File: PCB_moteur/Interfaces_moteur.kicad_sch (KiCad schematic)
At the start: 3 parts, among them Q1 BSS138, U3 LSF0102DCUR

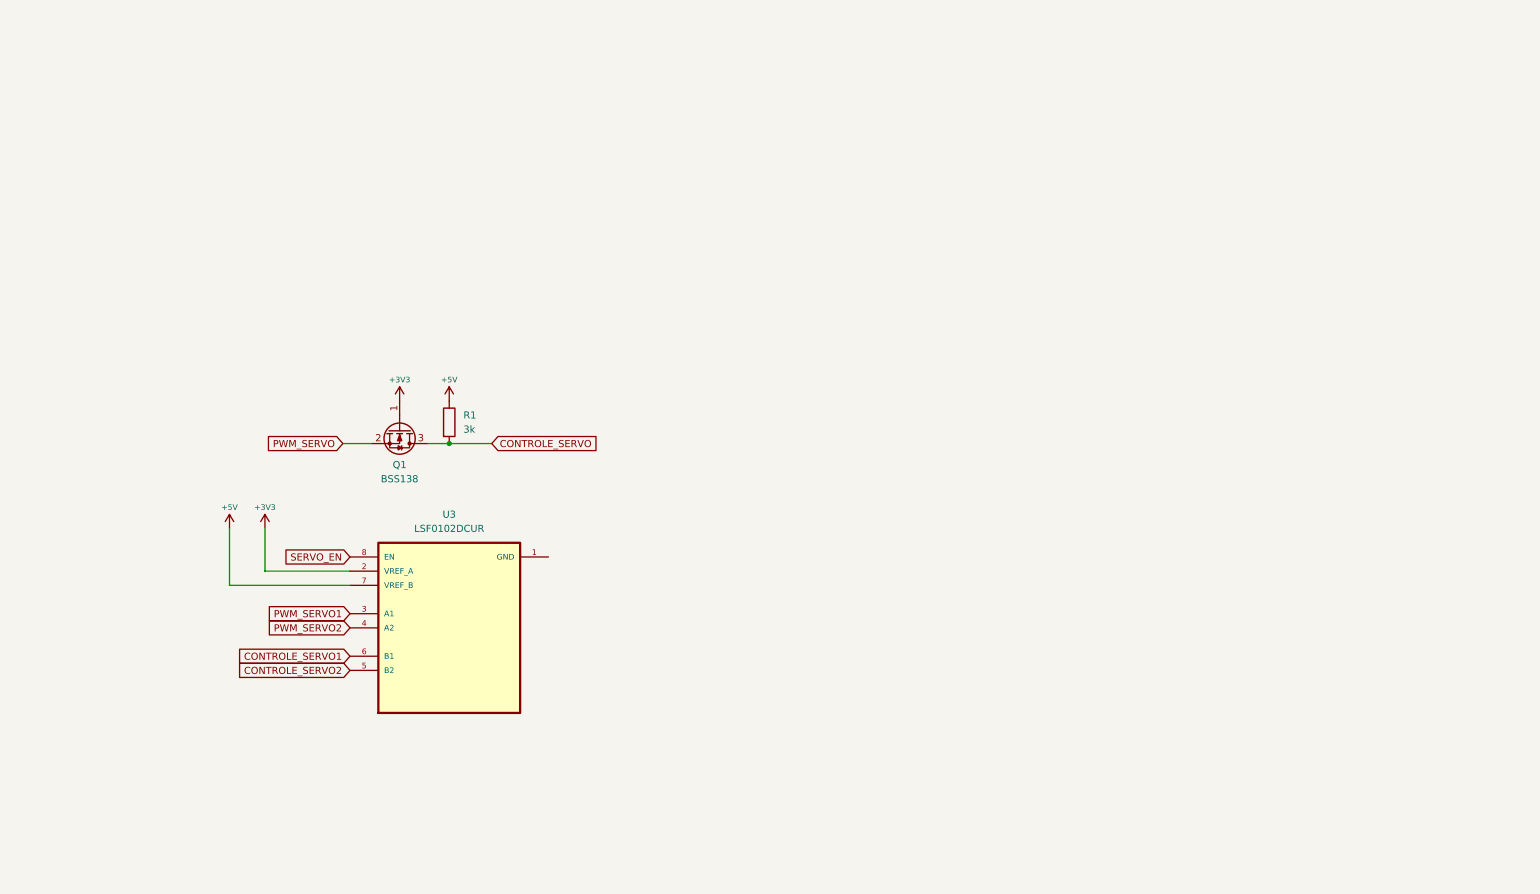
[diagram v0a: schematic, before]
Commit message: Manque supply, pyro et finition (découplage etc)
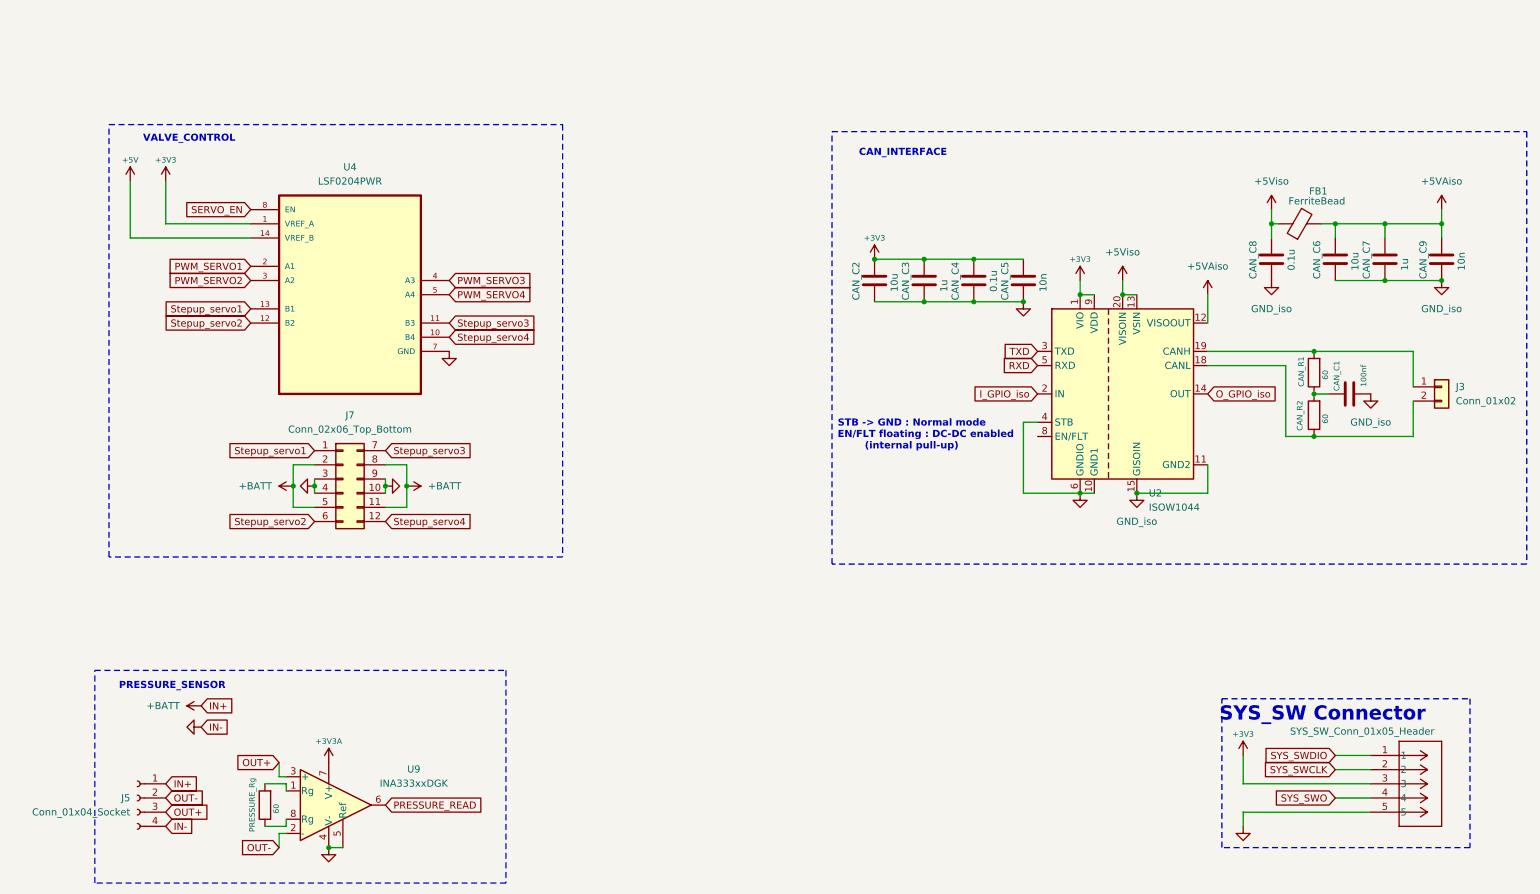
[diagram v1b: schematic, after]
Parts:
- removed Q1: BSS138, Package_TO_SOT_SMD:SOT-23, symbol Transistor_FET:BSS138
- removed R1: 3k, symbol Device:R
- removed U3: LSF0102DCUR, LSF0102DCUR:SOP50P310X90-8N, symbol LSF0102DCUR:LSF0102DCUR
- added CAN_C1: 100nf, Capacitor_SMD:C_0805_2012Metric, symbol Device:C
- added CAN_C2, CAN_C6: 10u, symbol Device:C
- added CAN_C3, CAN_C7: 1u, symbol Device:C
- added CAN_C4, CAN_C8: 0.1u, symbol Device:C
- added CAN_C5, CAN_C9: 10n, symbol Device:C
- added CAN_R1, CAN_R2, PRESSURE_Rg: 60, Resistor_SMD:R_0805_2012Metric, symbol Device:R
- added FB1: FerriteBead, symbol Device:FerriteBead
- added J3: Conn_01x02, symbol Connector_Generic:Conn_01x02
- added J4: SYS_SW_Conn_01x05_Header, Connector_PinHeader_2.54mm:PinHeader_1x05_P2.54mm_Vertical, symbol ODB2:705430004
- added J5: Conn_01x04_Socket, symbol Connector:Conn_01x04_Socket
- added J7: Conn_02x06_Top_Bottom, symbol Connector_Generic:Conn_02x06_Top_Bottom
- added U2: ISOW1044, Package_SO:SOIC-20W_7.5x12.8mm_P1.27mm, symbol Interface_CAN_LIN:ISOW1044
- added U4: LSF0204PWR, LSF0204PWR:SOP65P640X120-14N, symbol LSF0204PWR:LSF0204PWR
- added U9: INA333xxDGK, Package_SO:VSSOP-8_3x3mm_P0.65mm, symbol Amplifier_Instrumentation:INA333xxDGK
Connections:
- net +3V3: now also CAN_C2.1, CAN_C3.1, CAN_C4.1, CAN_C5.1, J4.3, U2.1 (VIO), U2.9 (VDD), U4.1 (VREF_A)
- net +5V: now also U4.14 (VREF_B)
- net PWM_SERVO1: now also U4.2 (A1)
- net PWM_SERVO2: now also U4.3 (A2)
- net SERVO_EN: now also U4.8 (EN)
- new net: PRESSURE_Rg.2, U9.1 (Rg)
- new net: PRESSURE_Rg.1, U9.8 (Rg)
- new net: CAN_R2.1, J3.2 (Pin_2), U2.18 (CANL)
- new net: CAN_C1.1, CAN_R1.1, CAN_R2.2
- new net: CAN_R1.2, J3.1 (Pin_1), U2.19 (CANH)
- new net +3V3A: U9.7 (V+)
- new net +5VAiso: CAN_C6.1, CAN_C7.1, CAN_C9.1, FB1.2, U2.12 (VISOOUT)
- new net +5Viso: CAN_C8.1, FB1.1, U2.13 (VSIN), U2.20 (VISOIN)
- new net +BATT: J5.1 (Pin_1), J7.11 (Pin_11), J7.2 (Pin_2), J7.5 (Pin_5), J7.8 (Pin_8)
- new net GND: CAN_C2.2, CAN_C3.2, CAN_C4.2, CAN_C5.2, J4.5, J5.4 (Pin_4), J7.10 (Pin_10), J7.3 (Pin_3), J7.4 (Pin_4), J7.9 (Pin_9), U2.10 (GND1), U2.4 (STB), U2.6 (GNDIO), U4.7 (GND), U9.4 (V-), U9.5 (Ref)
- new net GND_iso: CAN_C1.2, CAN_C6.2, CAN_C7.2, CAN_C8.2, CAN_C9.2, U2.11 (GND2), U2.15 (GISOIN), U2.16 (GISOIN), U2.17 (GISOIN)
- new net I_GPIO_iso: U2.2 (IN)
- new net OUT+: J5.3 (Pin_3), U9.3 (+)
- new net OUT-: J5.2 (Pin_2), U9.2 (-)
- new net O_GPIO_iso: U2.14 (OUT)
- new net PRESSURE_READ: U9.6
- new net PWM_SERVO3: U4.4 (A3)
- new net PWM_SERVO4: U4.5 (A4)
- new net RXD: U2.5 (RXD)
- new net SYS_SWCLK: J4.2
- new net SYS_SWDIO: J4.1
- new net SYS_SWO: J4.4
- new net Stepup_servo1: J7.1 (Pin_1), U4.13 (B1)
- new net Stepup_servo2: J7.6 (Pin_6), U4.12 (B2)
- new net Stepup_servo3: J7.7 (Pin_7), U4.11 (B3)
- new net Stepup_servo4: J7.12 (Pin_12), U4.10 (B4)
- new net TXD: U2.3 (TXD)
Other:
- note added: "CAN_INTERFACE"
- note added: "PRESSURE_SENSOR"
- note added: "STB -> GND : Normal mode EN/FLT floating : DC-DC enabled (internal pull-up)"
- note added: "SYS_SW Connector"
- note added: "VALVE_CONTROL"

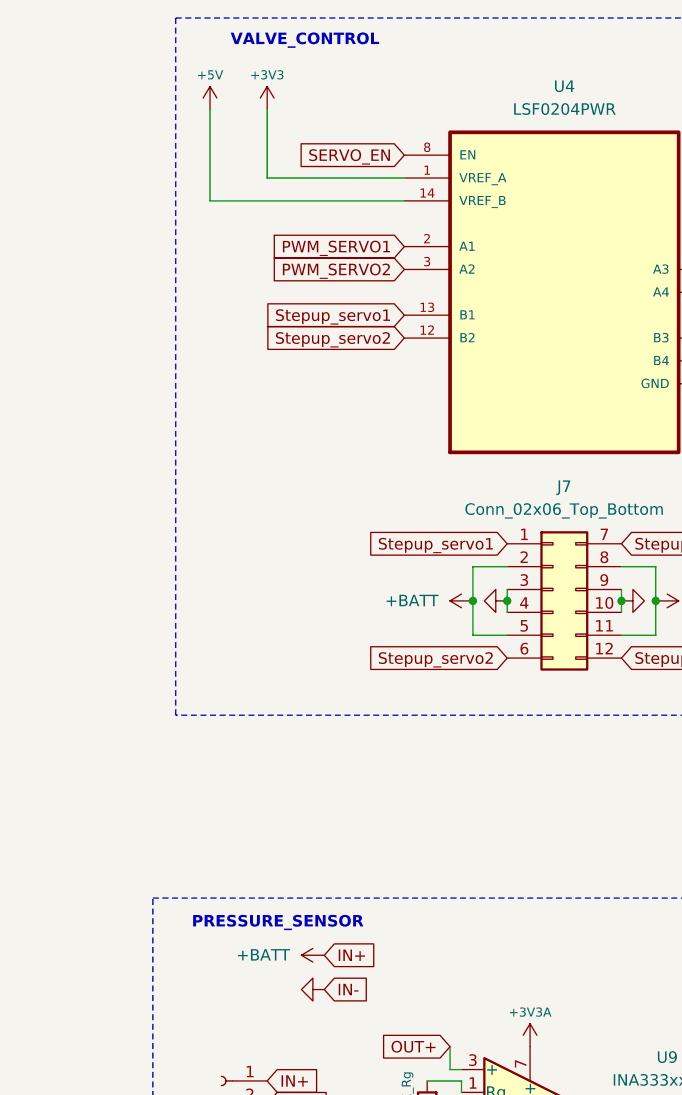
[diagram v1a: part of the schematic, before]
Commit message: wip: remove unnecessary components
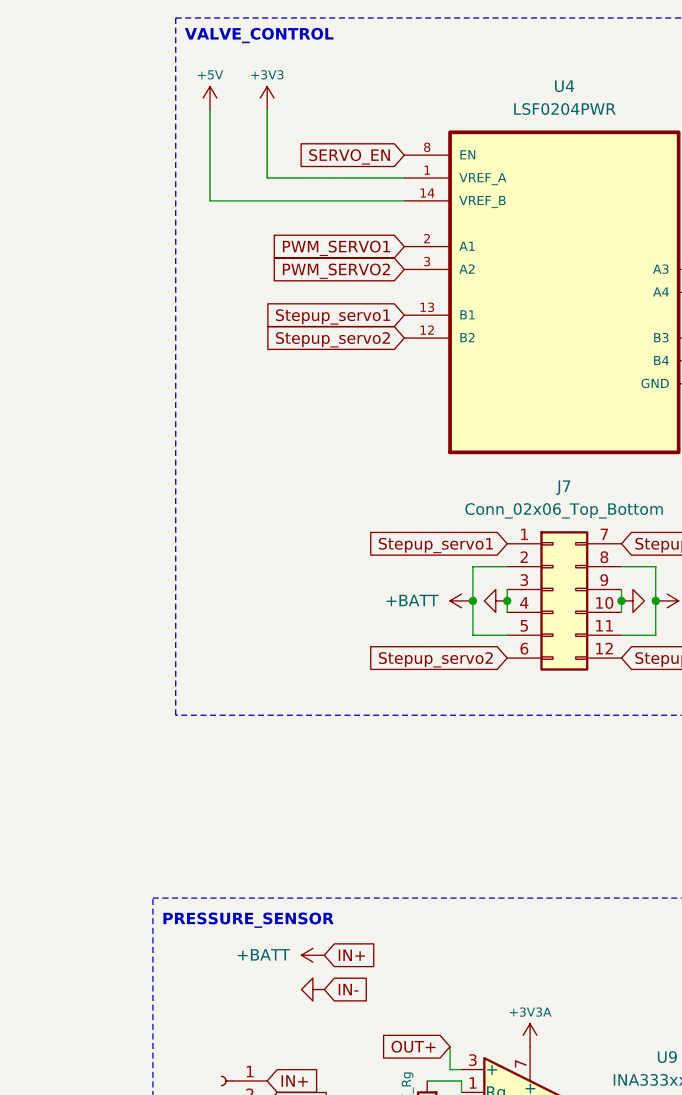
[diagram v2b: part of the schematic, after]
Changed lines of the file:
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@@
 	(text "VALVE_CONTROL\n"
 		(exclude_from_sim no)
-		(at 34.036 37.592 0)
+		(at 28.956 37.084 0)
 		(effects
 			(font
@@
 	(text "PRESSURE_SENSOR"
 		(exclude_from_sim no)
-		(at 29.718 135.636 0)
+		(at 26.416 135.382 0)
 		(effects
 			(font
